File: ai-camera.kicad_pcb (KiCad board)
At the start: 4 copper layers, 70 x 70 mm, 175 parts, among them J1 Conn-01x02_P2mm_S2B-PH-K-S_Ho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, J2 USB_B_Micro_10118194-0001LF, J3 DBG, J4 Conn-02x10_P2.54mm_B-2100S20P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, J5 Conn-01x02_P1.25mm_10114829-1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, J6 Conn_01x24_FFC_0.5mm_hirose_F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, Q1 AO3401A, Q2 AO3400A, Q3 AO3400A, Q4 AO3401A, Q5 AO3400A, Q6 AO3401A, Q7 AO3400A, Q8 AO3400A, SW1 SW_PB_90deg_K2-1102AQ-H4CW-01, SW2 SW_PB_TS-1187A-B-A-B, SW3 SW_PB_TS-1187A-B-A-B, SW4 SW_PB_90deg_K2-1102AQ-H4CW-01, U1 SRV05-4, U10 AP1511B, U11 ESP32-S3-WROOM-1-N16R8, U12 MT9284-28J, U13 APDS-9306-065, U2 TP4057-42-SOT26-R, U3 PCF8563T/5,518, U4 XC6206-2.8V, U5 PIR_BS612, U6 SY8089AAAC, U7 SOT-23-6_SN74LVC1G373DBVR_TI, U8 XC6206-2.8V, U9 RT9166-12GVL, Y1 32.768kHz_Q13FC1350000400

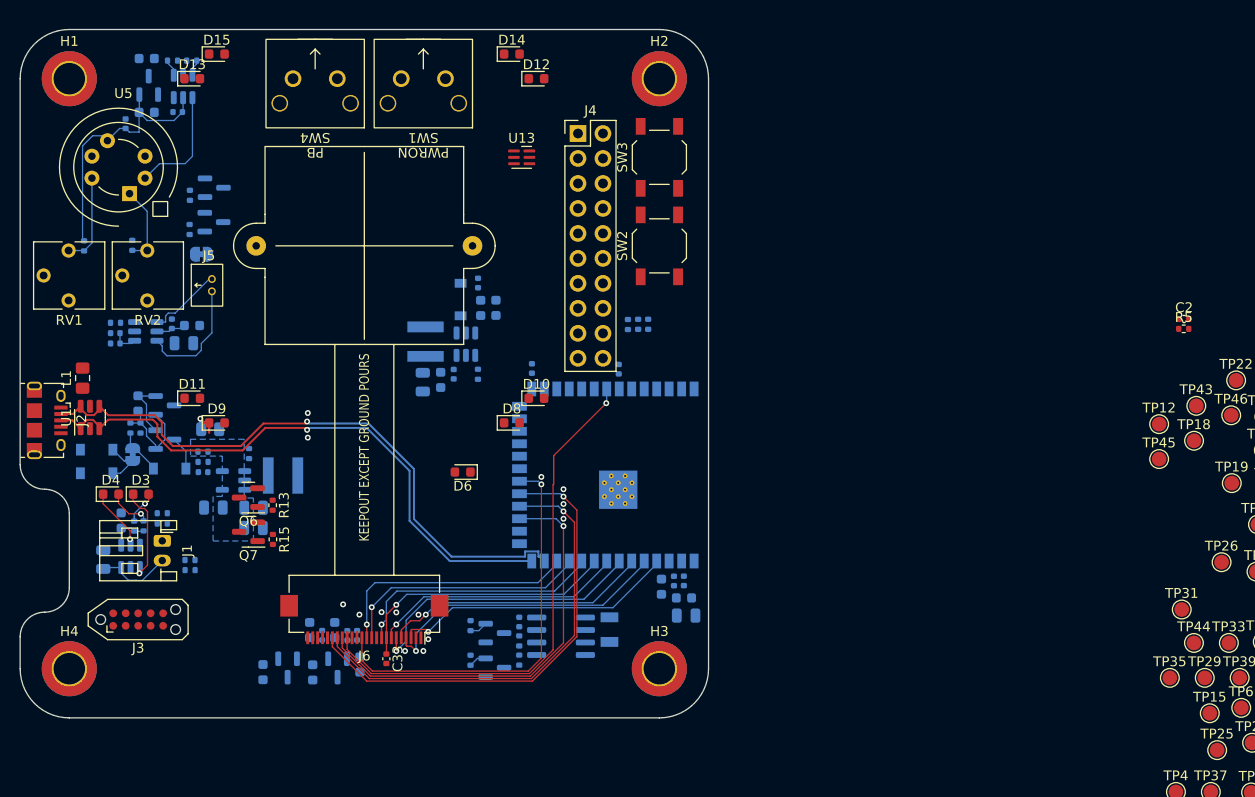
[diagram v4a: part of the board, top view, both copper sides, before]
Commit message: ai camera layout: route ground ring
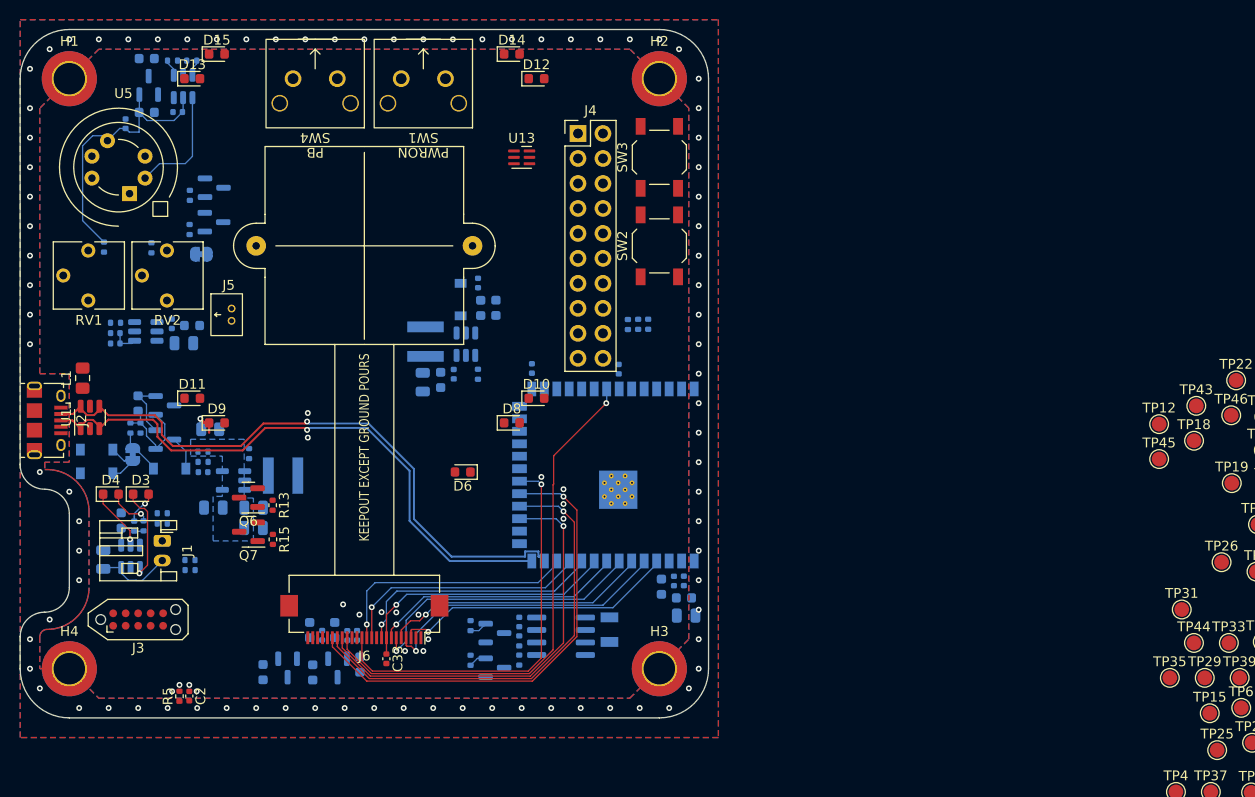
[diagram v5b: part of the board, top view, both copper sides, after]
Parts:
- moved R5 108.7 mm to (111.2, 112.8), turned to 90 degrees
- moved C2 108.2 mm to (112.2, 112.8), turned to -90 degrees
- moved J5 3.61 mm to (116.0, 74.0)
- moved R14 2.03 mm to (103.5, 67.1)
- moved RV1 2.00 mm to (101.9, 67.5)
- moved RV2 2.00 mm to (109.9, 67.5)
- moved R17 1.97 mm to (108.3, 67.2)
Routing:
- net Net-(J5-Pad1): track 12.1 -> 0.00 mm
- net Net-(R14-Pad2): track 9.32 -> 0.00 mm
- net Net-(R17-Pad2): track 8.06 -> 0.00 mm
- net Net-(J5-Pad2): track 7.77 -> 0.00 mm
- net +3V3: track 3.04 -> 0.00 mm
- net /PWR_PIR: track 27.5 -> 28.3 mm
- net GNDPWR: vias 0 -> 85
- net GND: vias 14 -> 18
- added copper zone on B.Cu, net GNDPWR
- added copper zone on F.Cu, net GNDPWR
- added copper zone on In1.Cu, net GNDPWR
- added copper zone on In2.Cu, net GNDPWR

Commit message: ai camera layout: battery and part of power circuit
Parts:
- C14: moved to F.Cu
- moved TP3 73.3 mm to (210.0, 50.0), turned to -90 degrees
- moved TP37 68.4 mm to (205.0, 55.0), turned to -90 degrees
- moved TP28 63.2 mm to (180.0, 80.0), turned to -90 degrees
- moved TP27 61.0 mm to (200.0, 60.0), turned to -90 degrees
- moved TP14 60.5 mm to (185.0, 85.0), turned to -90 degrees
- moved TP25 57.5 mm to (195.0, 65.0), turned to -90 degrees
- moved TP6 51.8 mm to (185.0, 75.0), turned to -90 degrees
- moved TP38 50.3 mm to (190.0, 80.0), turned to -90 degrees
- moved TP29 48.2 mm to (190.0, 70.0), turned to -90 degrees
- moved TP1 47.6 mm to (190.0, 90.0), turned to -90 degrees
- moved TP24 45.1 mm to (195.0, 85.0), turned to -90 degrees
- moved TP13 40.3 mm to (225.0, 95.0), turned to -90 degrees
- moved TP5 38.7 mm to (200.0, 70.0), turned to -90 degrees
- moved TP36 36.4 mm to (200.0, 100.0), turned to -90 degrees
- moved TP31 34.2 mm to (195.0, 75.0), turned to -90 degrees
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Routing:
- net /PWR_PIR: track 28.3 -> 0.00 mm
- net +BATT: track 7.77 -> 30.7 mm
- net +5P: track 0.00 -> 20.8 mm, vias 0 -> 1
- net Net-(U5-Pad2): track 11.7 -> 0.00 mm
- net /CAM.D9: track 41.6 -> 32.8 mm
- net /CAM.HREF: track 52.9 -> 46.0 mm
- net /CAM.D7: track 25.6 -> 18.9 mm
- net /CAM.MCLK: track 25.5 -> 18.8 mm
- net Net-(Q1-Pad2): track 6.48 -> 0.00 mm
- net /CAM.D4: track 29.0 -> 22.6 mm
- net /CAM.D8: track 25.3 -> 19.0 mm
- net /CAM.D3: track 30.2 -> 24.1 mm
- net /CAM.D5: track 27.3 -> 21.4 mm
- net /CAM.PCLK: track 27.6 -> 22.0 mm
- net /CAM.D2: track 29.2 -> 23.9 mm
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- added copper zone on B.Cu, net +5F
- added copper zone on F.Cu, net +5F
- added copper zone on B.Cu, net +BATT
- added copper zone on B.Cu, net Net-(D1-Pad1)
- added copper zone on F.Cu, net Net-(J2-Pad1)
- added copper zone on B.Cu, net VBUS

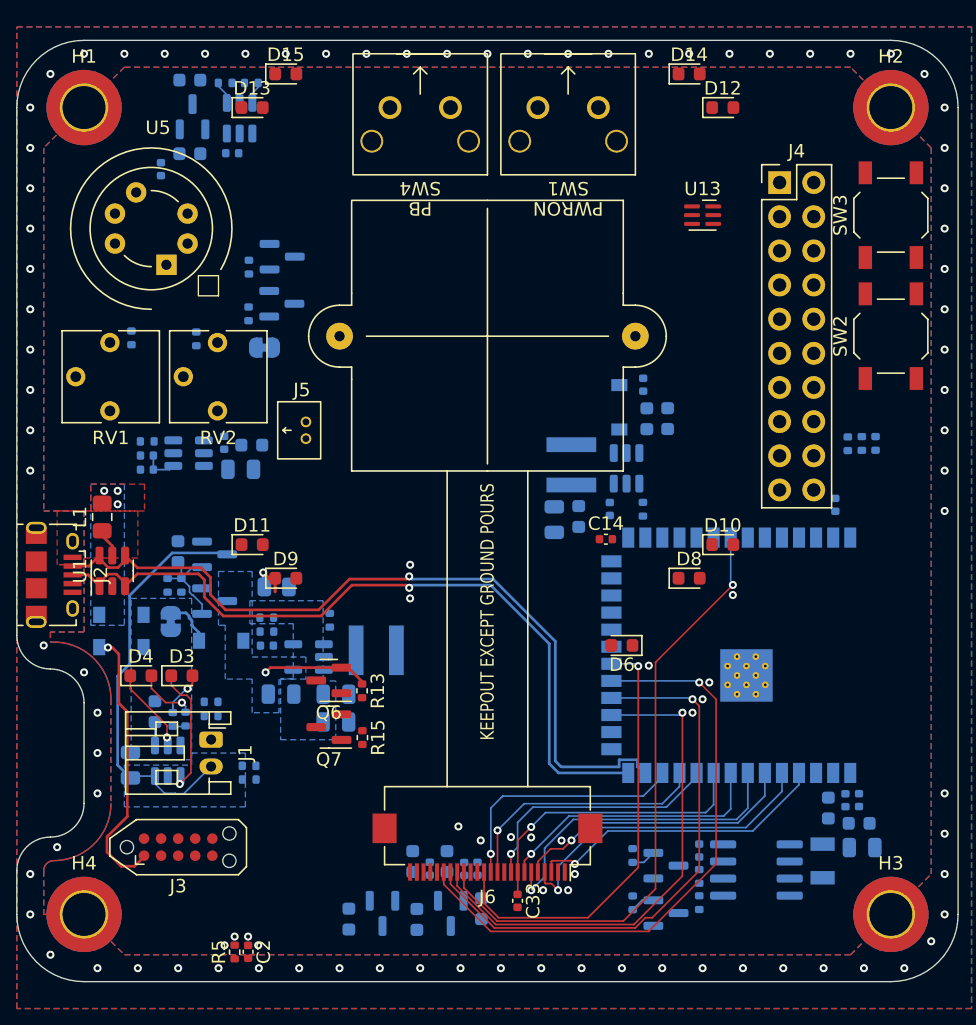
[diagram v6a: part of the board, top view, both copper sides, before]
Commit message: ai camera layout: route 3.3v, 5v
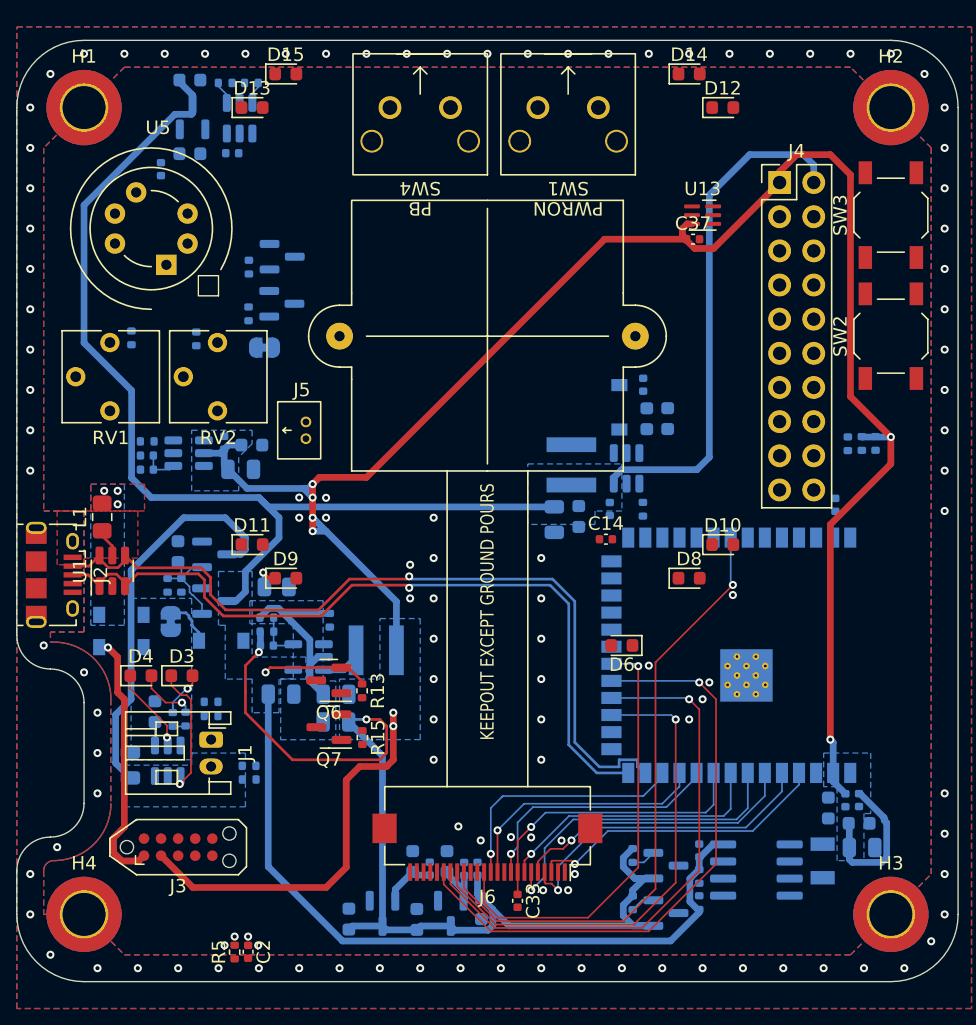
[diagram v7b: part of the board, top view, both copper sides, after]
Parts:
- added C37: 100n_0402_CL05B104KB54PNC, Capacitor_SMD:C_0402_1005Metric, F.Cu at (145.3, 59.8)
- renumbered C37 to C38, C38 to C39, C39 to C40, C40 to C41
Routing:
- net +3V3: track 0.00 -> 255.9 mm, vias 0 -> 10
- net VBUS: track 7.93 -> 179.4 mm
- net GND: track 0.00 -> 15.9 mm, vias 19 -> 36
- net +1V2: track 0.00 -> 4.56 mm
- net +2V8: track 0.00 -> 4.05 mm
- net Net-(C11-Pad2): track 0.00 -> 3.61 mm
- net Net-(U6-Pad3): track 0.00 -> 3.31 mm
- net +5P: track 20.8 -> 19.5 mm
- net +BATT: track 30.7 -> 29.5 mm
- net /CAM.PWDN: track 38.0 -> 36.8 mm
- net Net-(R30-Pad2): track 3.17 -> 2.17 mm
- net /UD+: track 57.2 -> 58.2 mm
- net /UD-: track 59.8 -> 60.7 mm
- added copper zone on B.Cu, net +3V3

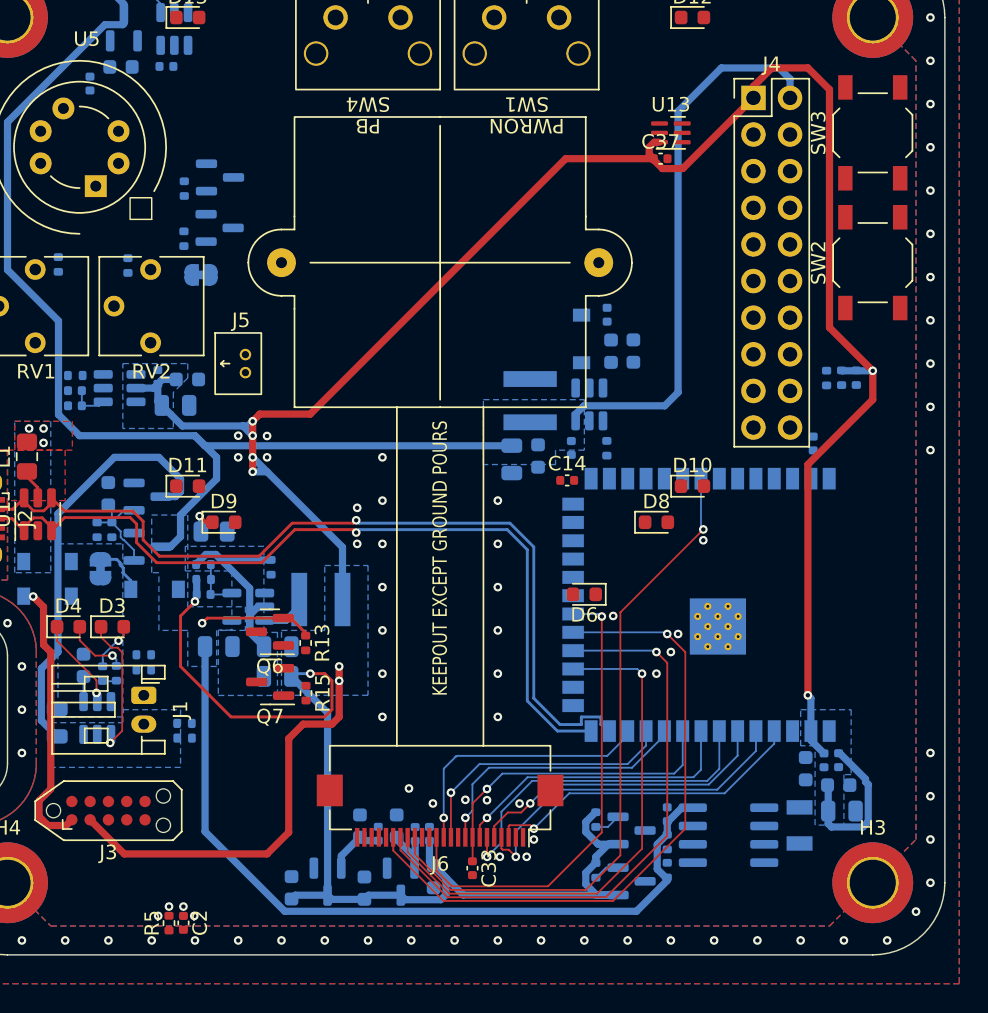
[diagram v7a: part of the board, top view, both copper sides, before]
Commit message: ai camera layout: route TX/RX/EN/BOOT
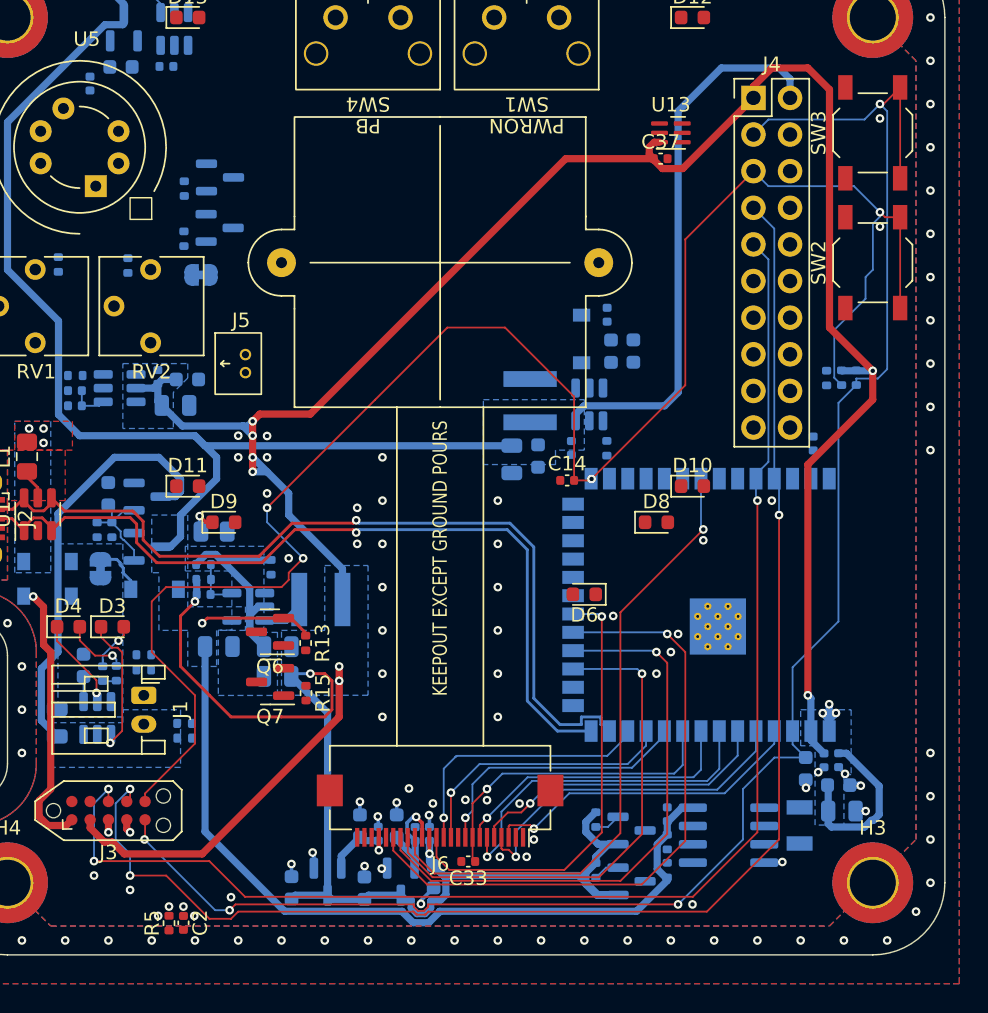
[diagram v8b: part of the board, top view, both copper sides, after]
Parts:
- moved C33 0.55 mm to (131.9, 108.5), turned to 180 degrees
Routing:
- net /ESP_BOOT: track 0.00 -> 125.9 mm, vias 0 -> 4
- net /ESP_EN: track 0.00 -> 123.6 mm, vias 0 -> 4
- net /TXD0: track 0.00 -> 101.0 mm, vias 0 -> 3
- net /RXD0: track 0.00 -> 96.8 mm, vias 0 -> 3
- net GND: track 15.9 -> 35.0 mm, vias 36 -> 65
- net +1V2: track 4.56 -> 8.44 mm, vias 0 -> 1
- net /CAM.HREF: track 46.0 -> 44.2 mm
- net +2V8: track 4.05 -> 5.62 mm, vias 0 -> 1
- net /CAM.PWDN: track 36.8 -> 35.3 mm
- net /CAM.D9: track 32.8 -> 31.3 mm
- net /CAM.VSYNC: track 41.4 -> 40.4 mm
- net VBUS: track 179.4 -> 180.1 mm
- net +3V3: track 255.9 -> 256.0 mm, vias 10 -> 11
